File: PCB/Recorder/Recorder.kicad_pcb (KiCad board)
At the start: 2 copper layers, 70 x 70 mm, 58 parts, among them J1 Reset, J3 TC2030-USB-NL-DS, J4 TF_PUSH, J5 USB-C-Socket-H, J6 Battery, Q1 CJ2301, SW1 SW_Push_DPDT, U1 ESP32-S3-MINI-1-N4R2, U2 TPS22916CNYFPR, U3 TP4054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

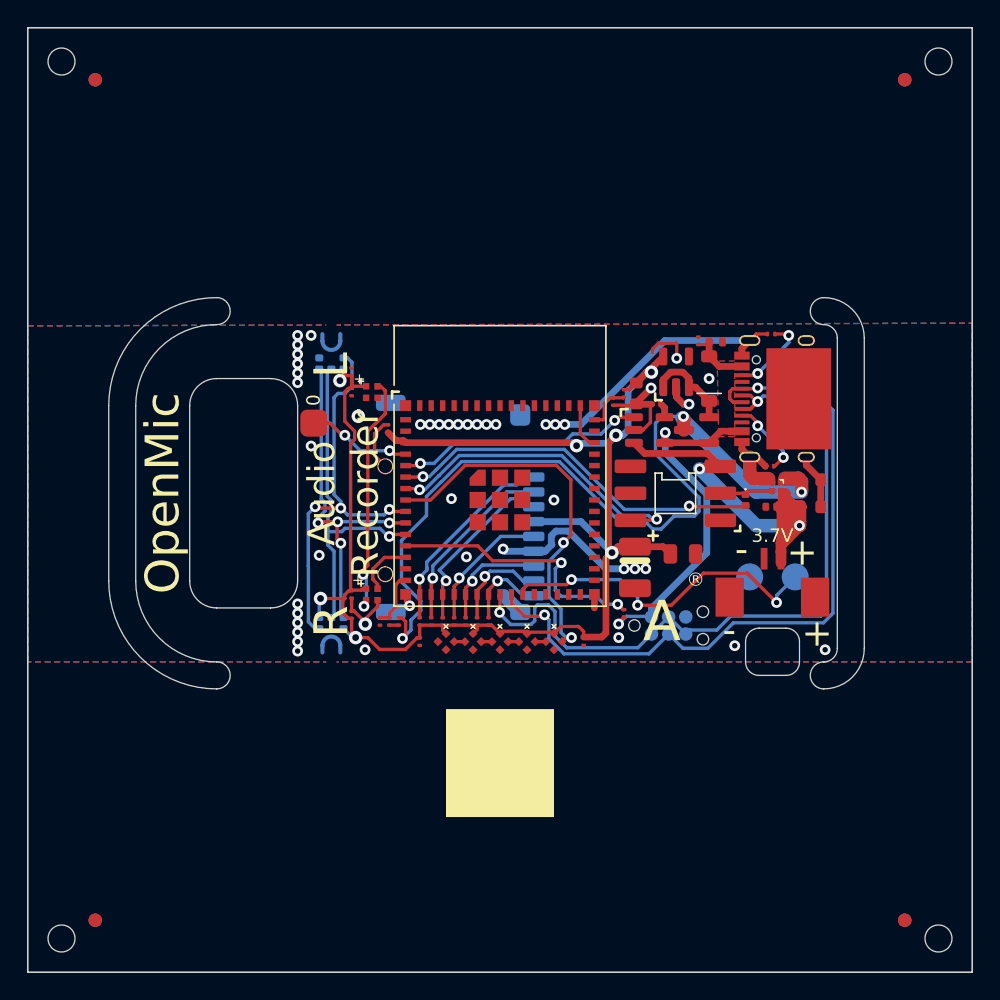
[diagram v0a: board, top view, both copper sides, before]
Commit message: New LEDs
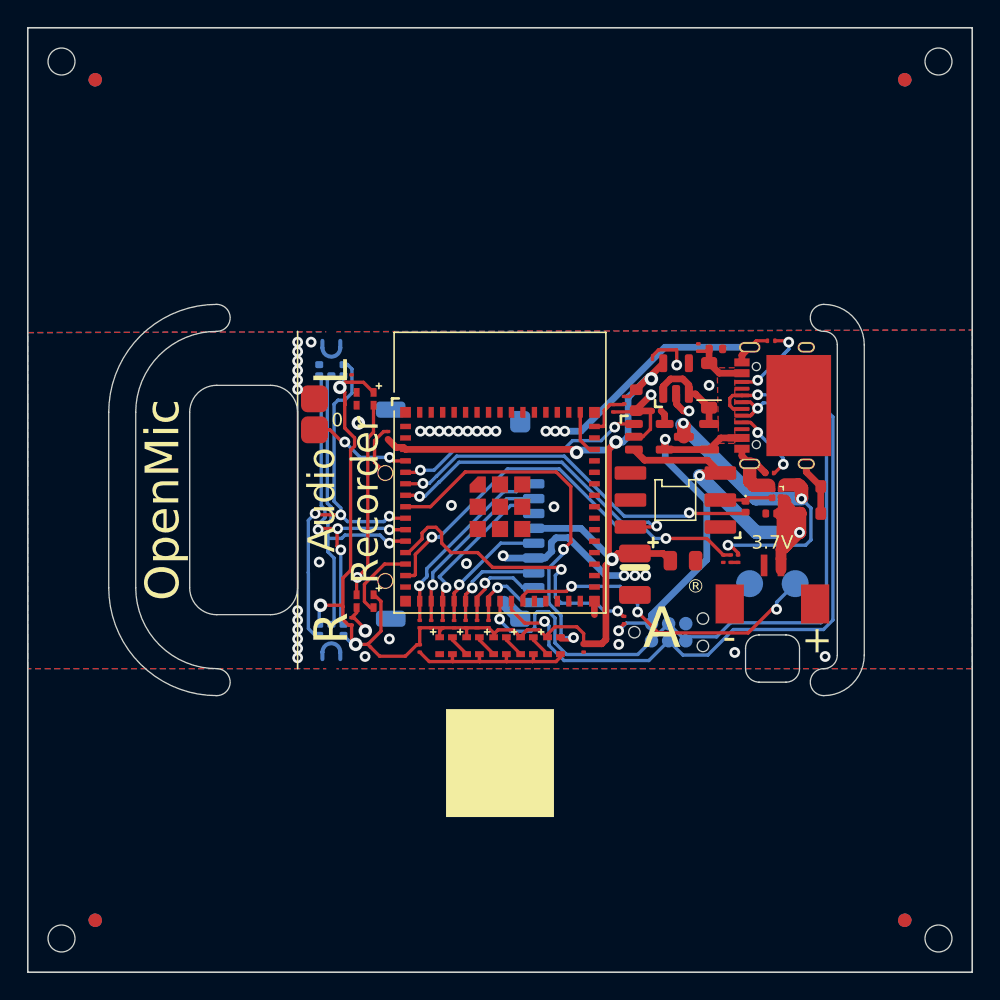
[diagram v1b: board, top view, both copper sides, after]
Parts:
- removed C13, C15: 100nF, RevK:C_0201
- added TP2: TestPoint, RevK:PAD-2mm, F.Cu at (86.2, 92.5)
- D10, D4, D5, D6, D7, D8, D9: footprint RevK:SMD1010 -> RevK:SMD1615
- moved R16 25.9 mm to (116.5, 104.3)
- moved R15 25.7 mm to (117.1, 104.3)
- moved R14 25.6 mm to (117.7, 104.3)
- moved D7 0.71 mm to (90.0, 107.5), turned to 0 degrees
- moved D9 0.71 mm to (90.0, 92.5), turned to 0 degrees
- moved TP1 0.50 mm to (86.2, 94.8)
- moved C1 0.50 mm to (123.0, 101.0)
- moved C10 0.50 mm to (89.0, 109.0)
- moved C11 0.50 mm to (89.0, 91.0)
- moved C12 0.50 mm to (94.0, 111.0)
- moved C14 0.50 mm to (106.2, 111.0)
- moved C2 0.50 mm to (108.4, 93.2)
- moved C3 0.50 mm to (123.0, 99.0)
- moved C4 0.50 mm to (91.7, 95.2)
- moved C5 0.50 mm to (110.1, 92.6)
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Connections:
- D10 pad 1: unconnected-(D10-O-Pad1) -> GND
- D10 pad 2: +3V3 -> Net-(D10-+)
- D10 pad 3: GND -> +3V3
- D10 pad 4: Net-(D10-I) -> unconnected-(D10-O-Pad4)
- D4 pad 1: Net-(D4-O) -> GND
- D4 pad 2: +3V3 -> BLINK
- D4 pad 3: GND -> +3V3
- D4 pad 4: BLINK -> Net-(D4-O)
- D5 pad 1: Net-(D5-O) -> GND
- D5 pad 2: +3V3 -> Net-(D4-O)
- D5 pad 3: GND -> +3V3
- D5 pad 4: Net-(D4-O) -> Net-(D5-I)
- D6 pad 1: Net-(D6-O) -> GND
- D6 pad 2: +3V3 -> Net-(D5-I)
- D6 pad 3: GND -> +3V3
- D6 pad 4: Net-(D5-O) -> Net-(D6-I)
- D7 pad 1: Net-(D7-O) -> GND
- D7 pad 2: +3V3 -> LEDMIC
- D7 pad 3: GND -> +3V3
- D7 pad 4: LEDMIC -> Net-(D7-I)
- D8 pad 1: Net-(D10-I) -> GND
- D8 pad 2: +3V3 -> Net-(D6-I)
- D8 pad 3: GND -> +3V3
- D8 pad 4: Net-(D6-O) -> Net-(D10-+)
- D9 pad 1: unconnected-(D9-O-Pad1) -> GND
- D9 pad 2: +3V3 -> Net-(D7-I)
- D9 pad 3: GND -> +3V3
- D9 pad 4: Net-(D7-O) -> unconnected-(D9-O-Pad4)
- U1 pad 14: unconnected-(U1-GPIO10-Pad14) -> ADC
- U1 pad 15: ADC -> unconnected-(U1-GPIO11-Pad15)
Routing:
- net VSWITCHED: track 62.6 -> 25.0 mm
- net ADC: track 4.21 -> 30.9 mm, vias 0 -> 2
- net Net-(D7-O): track 18.1 -> 0.00 mm, vias 2 -> 0
- net Net-(D7-I): track 0.00 -> 14.6 mm, vias 0 -> 1
- net GND: track 68.9 -> 78.3 mm, vias 45 -> 44
- net +3V3: track 108.5 -> 114.2 mm
- net Net-(U1-GPIO8): track 20.1 -> 22.2 mm
- net Net-(D6-I): track 0.00 -> 1.68 mm
- net Net-(D5-I): track 0.00 -> 1.68 mm
- net Net-(D10-+): track 0.00 -> 1.68 mm
- net LEDMIC: track 4.39 -> 5.81 mm
- net Net-(D4-O): track 0.80 -> 1.68 mm
- net Net-(D6-O): track 0.80 -> 0.00 mm
- net Net-(D5-O): track 0.80 -> 0.00 mm
- net Net-(D10-I): track 0.80 -> 0.00 mm
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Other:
- board text added: "1 2 3 5 6 7 9 10"
- board text removed: "1 2 3 5 6 7 9 11"

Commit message: Library update
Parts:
- turned SW1 to 0 degrees

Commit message: Manifest
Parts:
- moved J4 0.05 mm to (94.6, 101.0)
